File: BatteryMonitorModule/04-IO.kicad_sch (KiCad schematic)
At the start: 0 parts

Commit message: updated schematics — MCU and IO wiring updates, sheet instance fixes
Co-Authored-By: Claude Opus 4.6 (1M context) <noreply@anthropic.com>
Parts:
- added D3: 1N4148W, Diode_SMD:D_SOD-123, symbol Device:D_Schottky
- added J10: J_DISP_SPI, Connector_PinHeader_2.54mm:PinHeader_1x09_P2.54mm_Vertical, symbol Connector:Conn_01x09_Pin
- added J11: J_UART, Connector_PinHeader_2.54mm:PinHeader_1x04_P2.54mm_Vertical, symbol Connector:Conn_01x04_Pin
- added J12: J_EXP_A, Connector_PinHeader_2.54mm:PinHeader_1x05_P2.54mm_Vertical, symbol Connector:Conn_01x05_Pin
- added J13: J_EXP_B, Connector_PinHeader_2.54mm:PinHeader_1x08_P2.54mm_Vertical, symbol Connector:Conn_01x08_Pin
- added J5: J_FAN, Connector_PinHeader_2.54mm:PinHeader_1x02_P2.54mm_Vertical, symbol Connector:Conn_01x02_Pin
- added J6: J_FAN_SEL, Connector_PinHeader_2.54mm:PinHeader_1x03_P2.54mm_Vertical, symbol Connector:Conn_01x03_Pin
- added J7: J_NFC, Connector_PinHeader_2.54mm:PinHeader_1x04_P2.54mm_Vertical, symbol Connector:Conn_01x04_Pin
- added J8: J_PANEL, Connector_PinHeader_2.54mm:PinHeader_1x06_P2.54mm_Vertical, symbol Connector:Conn_01x06_Pin
- added J9: J_DISP_I2C, Connector_PinHeader_2.54mm:PinHeader_1x04_P2.54mm_Vertical, symbol Connector:Conn_01x04_Pin
- added LED1, LED2: WS2812B, LED_SMD:LED_WS2812B_PLCC4_5.0x5.0mm_P3.2mm, symbol LED:WS2812B
- added LED3: LED_12V, LED_SMD:LED_0603_1608Metric, symbol Device:LED
- added LED4: LED_3V3, LED_SMD:LED_0603_1608Metric, symbol Device:LED
- added LED5: LED_5V, LED_SMD:LED_0603_1608Metric, symbol Device:LED
- added LED6: LED_MCU, LED_SMD:LED_0603_1608Metric, symbol Device:LED
- added Q5: 2N7002, Package_TO_SOT_SMD:SOT-23, symbol Transistor_FET:BSS138
- added R16, R17, R18, R19, R20, R21: DNP, Resistor_SMD:R_0603_1608Metric, symbol Device:R
- added R22: 100R, Resistor_SMD:R_0603_1608Metric, symbol Device:R
- added R23: 100k, Resistor_SMD:R_0603_1608Metric, symbol Device:R
- added R24: 470R, Resistor_SMD:R_0603_1608Metric, symbol Device:R
- added R29: 2k, Resistor_SMD:R_0603_1608Metric, symbol Device:R
- added R30, R34: 270R, Resistor_SMD:R_0603_1608Metric, symbol Device:R
- added R31: 560R, Resistor_SMD:R_0603_1608Metric, symbol Device:R
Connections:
- new net: LED5.1 (K), R31.2
- new net: D3.2 (A), J5.1 (Pin_1), Q5.3 (D)
- new net: D3.1 (K), J5.2 (Pin_2), J6.2 (Pin_2)
- new net: LED3.1 (K), R29.2
- new net: LED1.2 (DOUT), LED2.4 (DIN)
- new net: LED4.1 (K), R30.2
- new net: LED6.1 (K), R34.2
- new net: LED1.4 (DIN), R24.2
- new net: Q5.1 (G), R22.2, R23.1
- new net +12V: J6.1 (Pin_1), LED3.2 (A), R20.1
- new net +3.3V: J10.8 (Pin_8), J11.2 (Pin_2), J12.4 (Pin_4), J13.6 (Pin_6), J7.2 (Pin_2), J8.4 (Pin_4), J9.2 (Pin_2), LED4.2 (A)
- new net +5V: J6.3 (Pin_3), LED1.1 (VDD), LED2.1 (VDD), LED5.2 (A)
- new net ADC_12V: R20.2, R21.1
- new net ADC_BAT: R16.2, R17.1
- new net ADC_CHG: R18.2, R19.1
- new net BAT_P_FUSED: R16.1
- new net BL_PWM: J10.1 (Pin_1)
- new net CHG_P_F2: R18.1
- new net FAN_PWM: R22.1
- new net GND: J10.9 (Pin_9), J11.3 (Pin_3), J12.5 (Pin_5), J13.7 (Pin_7), J7.3 (Pin_3), J8.5 (Pin_5), J9.3 (Pin_3), LED1.3 (VSS), LED2.3 (VSS), Q5.2 (S), R17.2, R19.2, R21.2, R23.2, R29.1, R30.1, R31.1, R34.1
- new net I2C1_SCL: J7.1 (Pin_1)
- new net I2C2_SCL: J9.1 (Pin_1)
- new net LED_DATA: R24.1
- new net LED_DATA_O: LED2.2 (DOUT)
- new net MCU_HB: LED6.2 (A)
- new net SPI2_CS: J10.4 (Pin_4)
- new net SPI2_DC: J10.3 (Pin_3)
- new net SPI2_MISO: J10.5 (Pin_5)
- new net SPI2_MOSI: J10.6 (Pin_6)
- new net SPI2_RST: J10.2 (Pin_2)
- new net SPI2_SCK: J10.7 (Pin_7)
- new net SW_A: J8.3 (Pin_3)
- new net SW_B: J8.2 (Pin_2)
- new net SW_C: J8.1 (Pin_1)
- new net USART2_TX: J11.1 (Pin_1)
- new net spare_J12-0: J12.3 (Pin_3)
- new net spare_J12-1: J12.2 (Pin_2)
- new net spare_J12-2: J12.1 (Pin_1)
- new net spare_J13-0: J13.5 (Pin_5)
- new net spare_J13-1: J13.4 (Pin_4)
- new net spare_J13-2: J13.3 (Pin_3)
- new net spare_J13-3: J13.2 (Pin_2)
- new net spare_J13-4: J13.1 (Pin_1)
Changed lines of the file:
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@@
-(kicad_sch
-	(version 20250114)
-	(generator "eeschema")
-	(generator_version "9.0")
-	(paper "A4")
-	(title_block
-		(title "Battery Monitor Module — 04-IO")
-		(rev "0.1")
-	)
-)

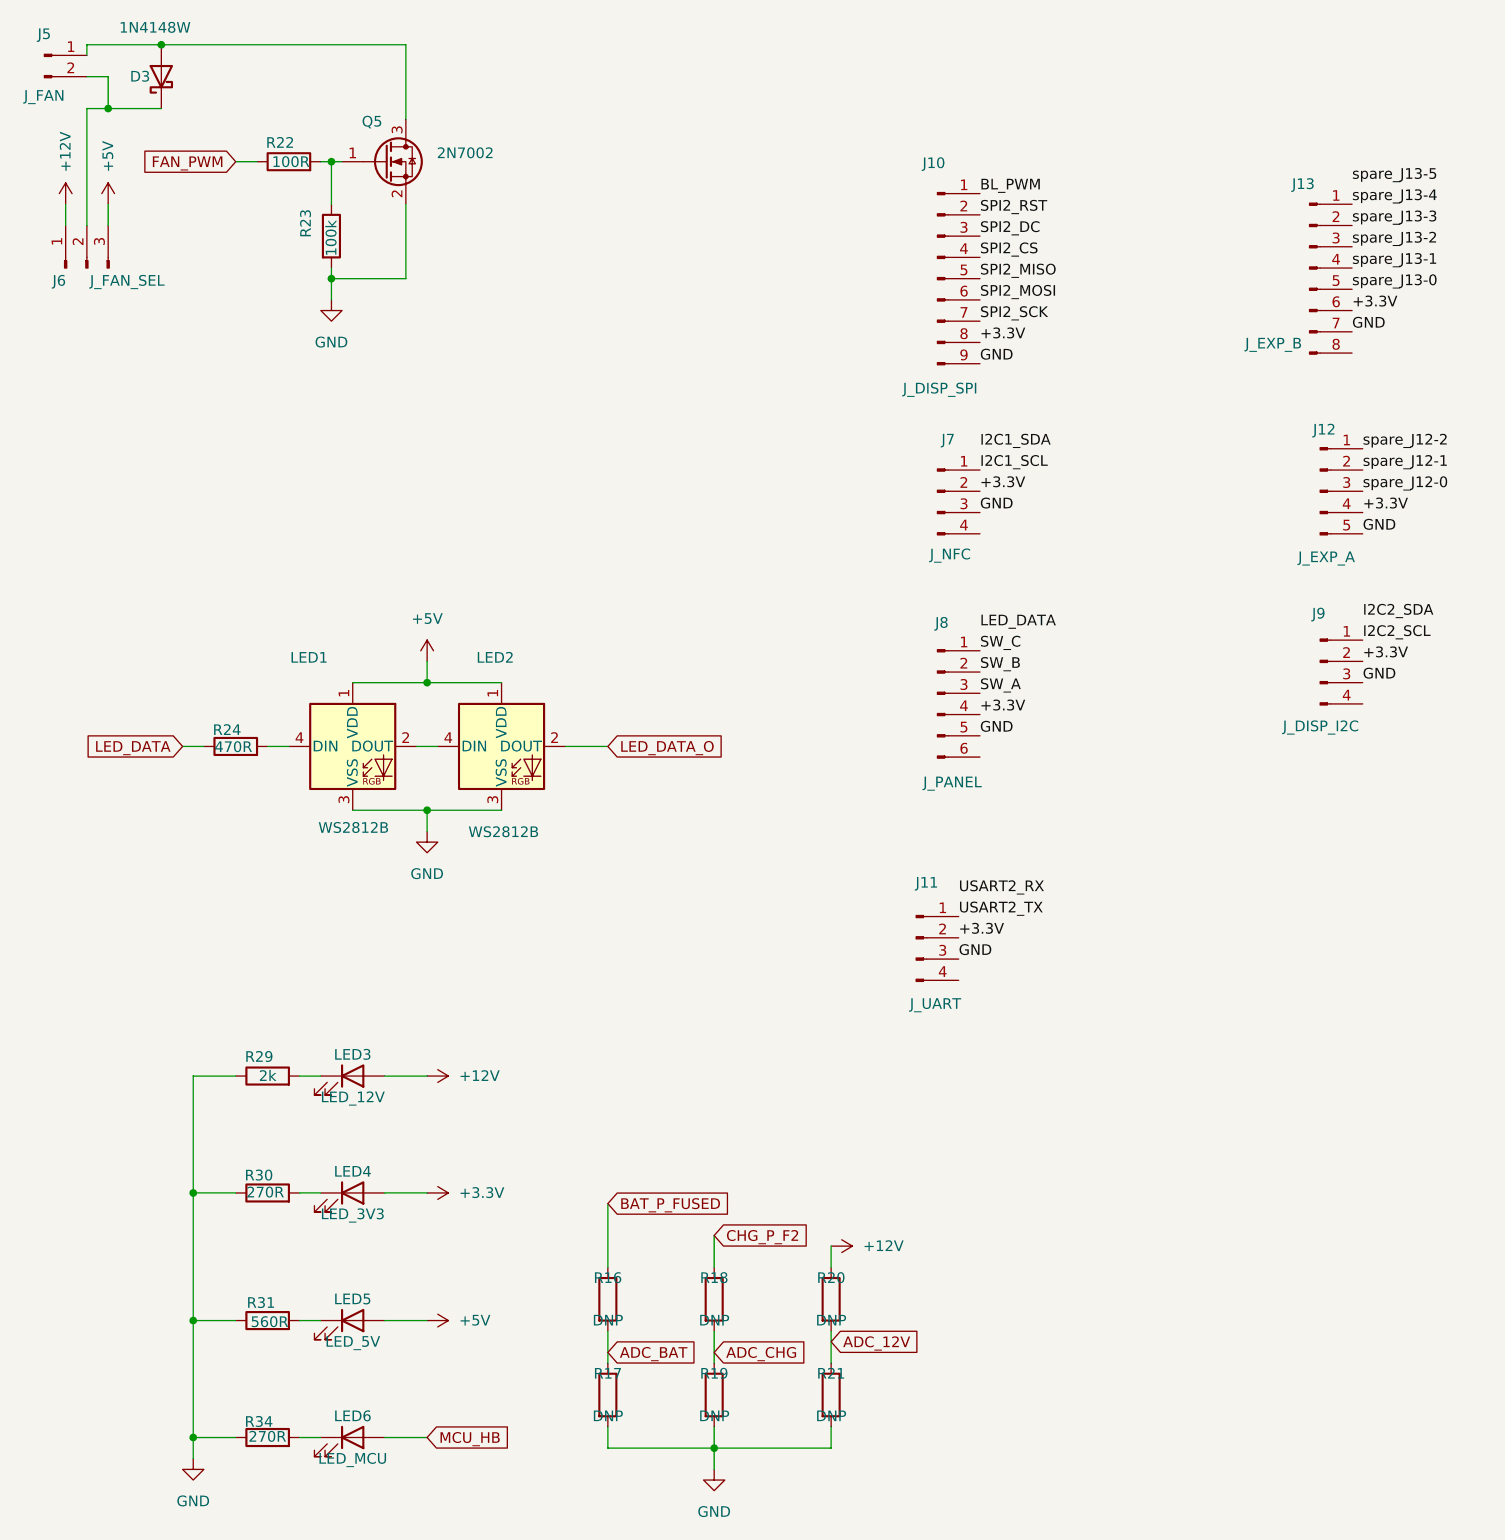
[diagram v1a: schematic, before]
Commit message: updated all schematics — IO sheet wiring, MCU connections, power supply refinements, custom footprints
Co-Authored-By: Claude Opus 4.6 (1M context) <noreply@anthropic.com>
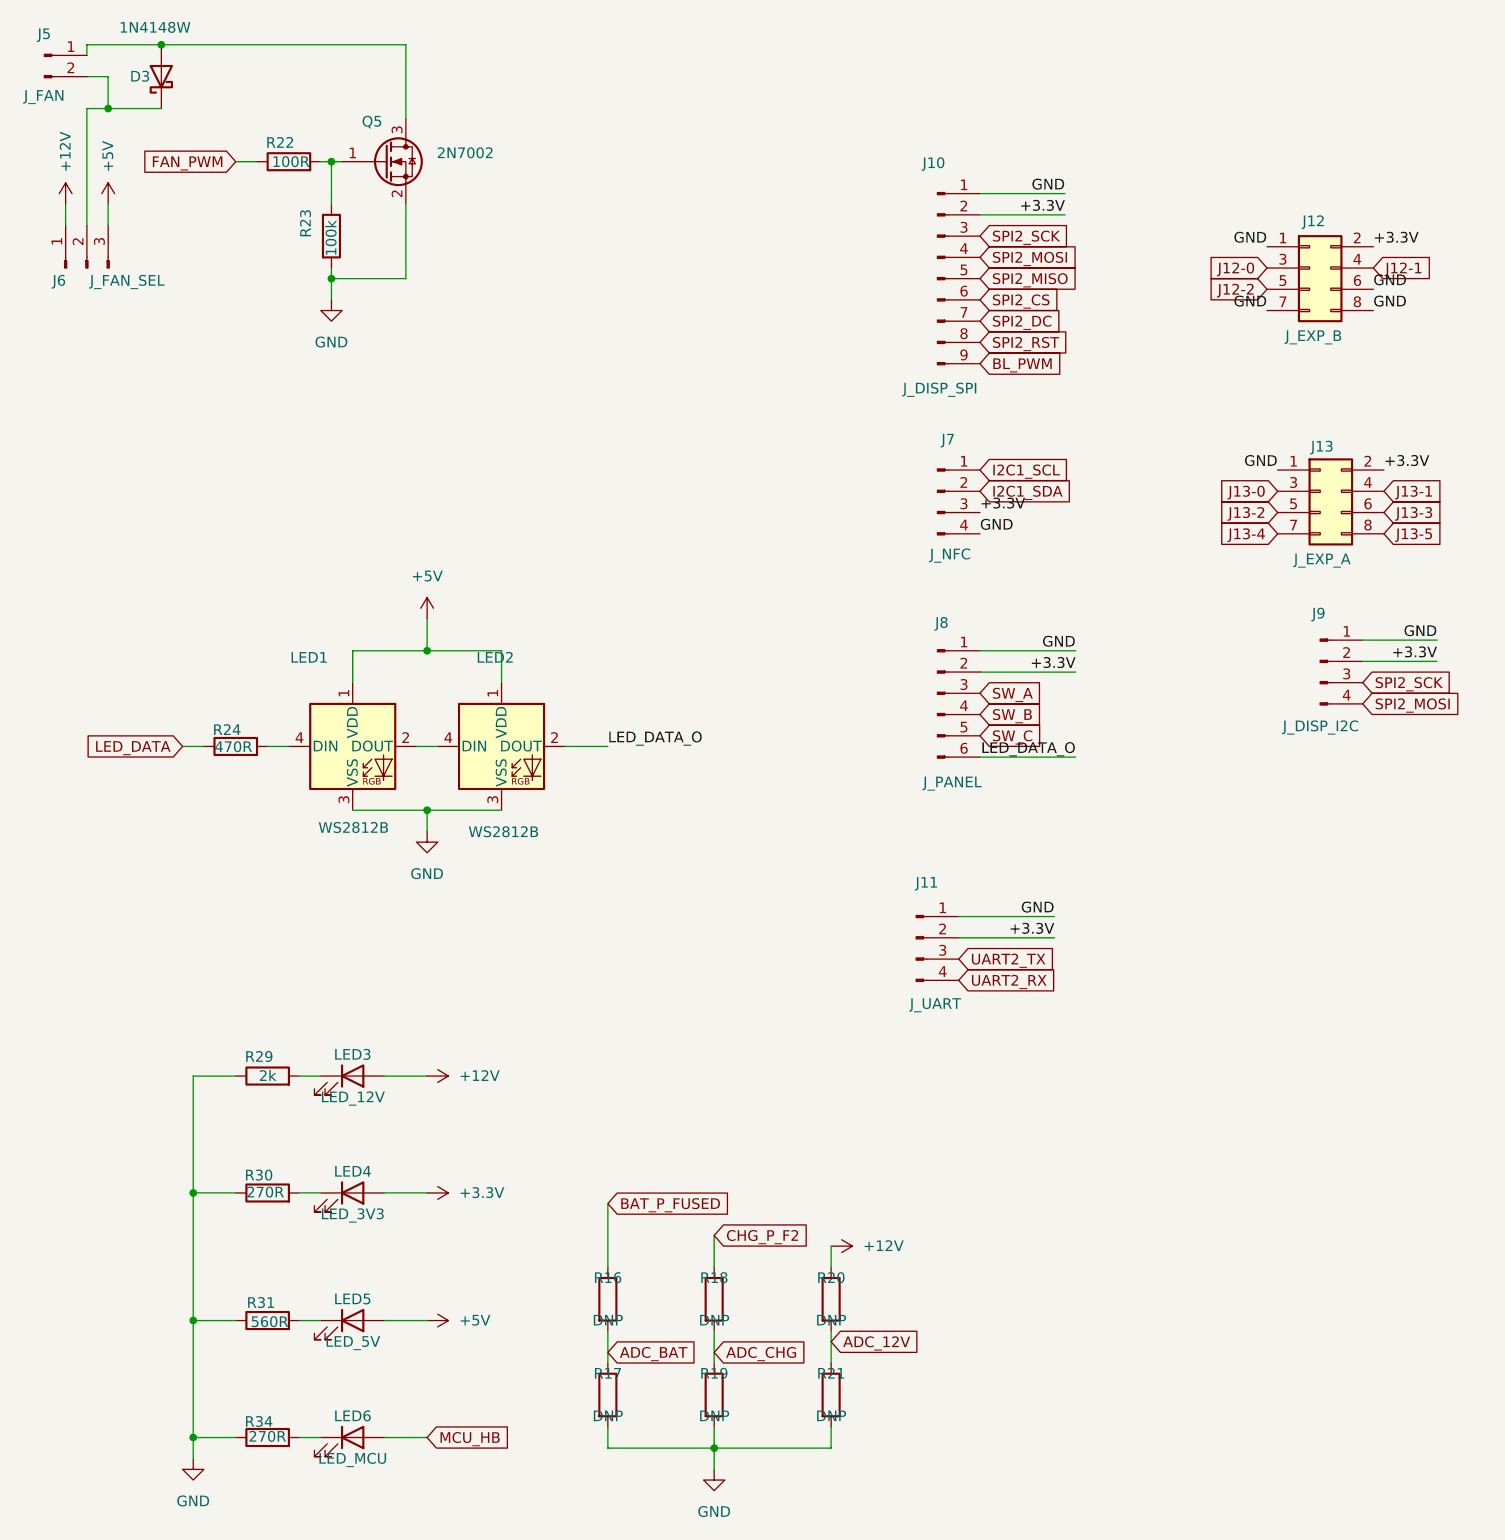
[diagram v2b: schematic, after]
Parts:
- removed J12: J_EXP_A, Connector_PinHeader_2.54mm:PinHeader_1x05_P2.54mm_Vertical, symbol Connector:Conn_01x05_Pin
- removed J13: J_EXP_B, Connector_PinHeader_2.54mm:PinHeader_1x08_P2.54mm_Vertical, symbol Connector:Conn_01x08_Pin
- added J12: J_EXP_B, Connector_PinHeader_2.54mm:PinHeader_2x04_P2.54mm_Vertical, symbol Connector_Generic:Conn_02x04_Odd_Even
- added J13: J_EXP_A, Connector_PinHeader_2.54mm:PinHeader_2x04_P2.54mm_Vertical, symbol Connector_Generic:Conn_02x04_Odd_Even
- J10: footprint Connector_PinHeader_2.54mm:PinHeader_1x09_P2.54mm_Vertical -> Connector_JST:JST_XH_B9B-XH-A_1x09_P2.50mm_Vertical
- J7, J9: footprint Connector_PinHeader_2.54mm:PinHeader_1x04_P2.54mm_Vertical -> Connector_JST:JST_XH_B4B-XH-A_1x04_P2.50mm_Vertical
- J8: footprint Connector_PinHeader_2.54mm:PinHeader_1x06_P2.54mm_Vertical -> Connector_JST:JST_XH_B6B-XH-A_1x06_P2.50mm_Vertical
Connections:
- net I2C2_SCL is gone; now on net GND: J9.1 (Pin_1)
- net USART2_TX is gone; now on net GND: J11.1 (Pin_1)
- net +3.3V: now also J10.2 (Pin_2), J7.3 (Pin_3), J8.2 (Pin_2), J12.2 (Pin_2), J13.2 (Pin_2); no longer J10.8 (Pin_8), J7.2 (Pin_2), J8.4 (Pin_4)
- net BL_PWM: now also J10.9 (Pin_9); no longer J10.1 (Pin_1)
- net GND: now also J10.1 (Pin_1), J7.4 (Pin_4), J8.1 (Pin_1), J12.1 (Pin_1), J12.6 (Pin_6), J12.7 (Pin_7), J12.8 (Pin_8), J13.1 (Pin_1); no longer J10.9 (Pin_9), J11.3 (Pin_3), J7.3 (Pin_3), J8.5 (Pin_5), J9.3 (Pin_3)
- net I2C1_SDA: now also J7.2 (Pin_2)
- net LED_DATA_O: now also J8.6 (Pin_6)
- net SPI2_CS: now also J10.6 (Pin_6); no longer J10.4 (Pin_4)
- net SPI2_DC: now also J10.7 (Pin_7); no longer J10.3 (Pin_3)
- net SPI2_MOSI: now also J10.4 (Pin_4), J9.4 (Pin_4); no longer J10.6 (Pin_6)
- net SPI2_RST: now also J10.8 (Pin_8); no longer J10.2 (Pin_2)
- net SPI2_SCK: now also J10.3 (Pin_3), J9.3 (Pin_3); no longer J10.7 (Pin_7)
- net SW_B: now also J8.4 (Pin_4); no longer J8.2 (Pin_2)
- net SW_C: now also J8.5 (Pin_5); no longer J8.1 (Pin_1)
- net UART2_RX: now reaches J11.4 (Pin_4)
- new net J12-0: J12.3 (Pin_3)
- new net J12-1: J12.4 (Pin_4)
- new net J12-2: J12.5 (Pin_5)
- new net J13-0: J13.3 (Pin_3)
- new net J13-1: J13.4 (Pin_4)
- new net J13-2: J13.5 (Pin_5)
- new net J13-3: J13.6 (Pin_6)
- new net J13-4: J13.7 (Pin_7)
- new net J13-5: J13.8 (Pin_8)
- new net UART2_TX: J11.3 (Pin_3)
